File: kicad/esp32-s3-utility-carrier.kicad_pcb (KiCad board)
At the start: 2 copper layers, 90 x 65 mm, 27 parts, among them SW1 BTN1, SW2 BTN2, SW3 BTN3, U2 SN74AHCT125N

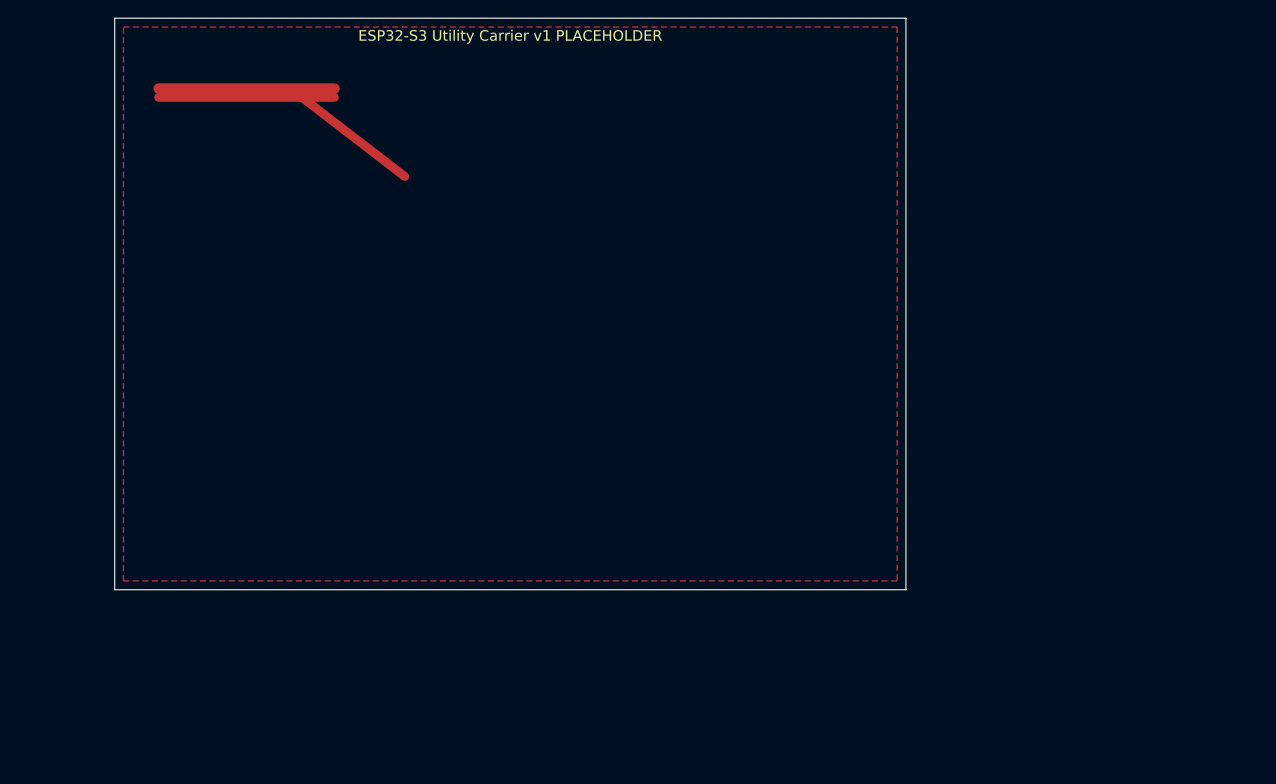
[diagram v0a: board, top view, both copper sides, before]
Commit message: feat(pcb): add optional W5500 ethernet header
v0.2 placeholder: J_W5500 (NOT POPULATED), 4 LED outputs via AHCT,
SPI on GPIO5/13/14/47/4/39 without pin conflicts; docs and generator updated.

Co-authored-by: Cursor <cursoragent@cursor.com>
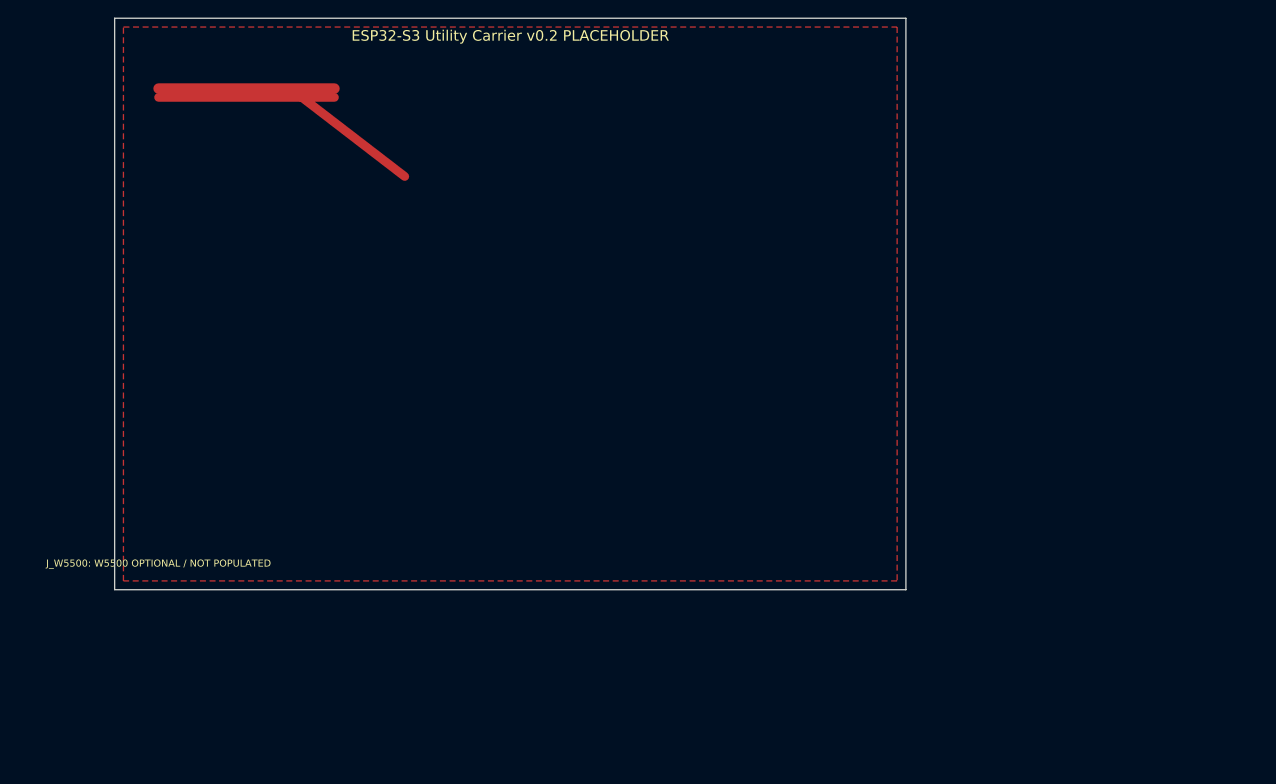
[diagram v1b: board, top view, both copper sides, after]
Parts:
- removed J_GPIO: GPIO, carrier:JST_XH_1x08_Placeholder
- added J_W5500: W5500_OPT_NP, carrier:JST_W5500_1x08_Placeholder, F.Cu at (5.00, 62.0)
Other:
- board text added: "ESP32-S3 Utility Carrier v0.2 PLACEHOLDER"
- board text added: "J_W5500: W5500 OPTIONAL / NOT POPULATED"
- board text removed: "ESP32-S3 Utility Carrier v1 PLACEHOLDER"
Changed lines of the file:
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@@
   (net 25 "ENC_DT")
   (net 26 "ENC_SW")
+  (net 27 "SPI_SCK")
+  (net 28 "SPI_MOSI")
+  (net 29 "SPI_MISO")
+  (net 30 "ETH_CS")
+  (net 31 "ETH_RST")
+  (net 32 "ETH_INT")
   (gr_rect (start 0 0) (end 90 65) (stroke (width 0.15) (type default)) (fill none) (layer "Edge.Cuts"))
   (gr_rect (start 28 8) (end 62 58) (stroke (width 0.2) (type default)) (fill none) (layer "Dwgs.User"))
@@
   (gr_text "ANTENNA KEEP-OUT" (at 45 64 0) (layer "Dwgs.User")
     (effects (font (size 0.9 0.9) (thickness 0.12))))
-  (gr_text "ESP32-S3 Utility Carrier v1 PLACEHOLDER" (at 45 2 0) (layer "F.SilkS")
+  (gr_text "ESP32-S3 Utility Carrier v0.2 PLACEHOLDER" (at 45 2 0) (layer "F.SilkS")
     (effects (font (size 1.2 1.2) (thickness 0.15))))
+  (gr_text "J_W5500: W5500 OPTIONAL / NOT POPULATED" (at 5 62 0) (layer "F.SilkS")
+    (effects (font (size 0.8 0.8) (thickness 0.1))))
   (footprint "carrier:JST_VH_1x02_Placeholder" (version 20240108) (generator "pcbnew")
     (layer "F.Cu") (at 5 8)
@@
     (attr through_hole)
   )
-  (footprint "carrier:JST_XH_1x08_Placeholder" (version 20240108) (generator "pcbnew")
-    (layer "F.Cu") (at 70 62)
-    (descr "") (tags "") (property "Reference" "J_GPIO")
-    (property "Value" "GPIO")
-    (property "Footprint" "carrier:JST_XH_1x08_Placeholder")
-    (attr through_hole)
-  )
+  (footprint "carrier:JST_W5500_1x08_Placeholder" (version 20240108) (generator "pcbnew")
+    (layer "F.Cu") (at 5 62)
+    (descr "") (tags "") (property "Reference" "J_W5500")
+    (property "Value" "W5500_OPT_NP")
+    (property "Footprint" "carrier:JST_W5500_1x08_Placeholder")
+    (attr through_hole)
+  )

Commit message: fix(pcb): clean up placeholder layout
Reorganize zones, keep connectors inside outline, add zone silk labels,
remove diagonal placeholder copper; layout verified in generator.

Co-authored-by: Cursor <cursoragent@cursor.com>
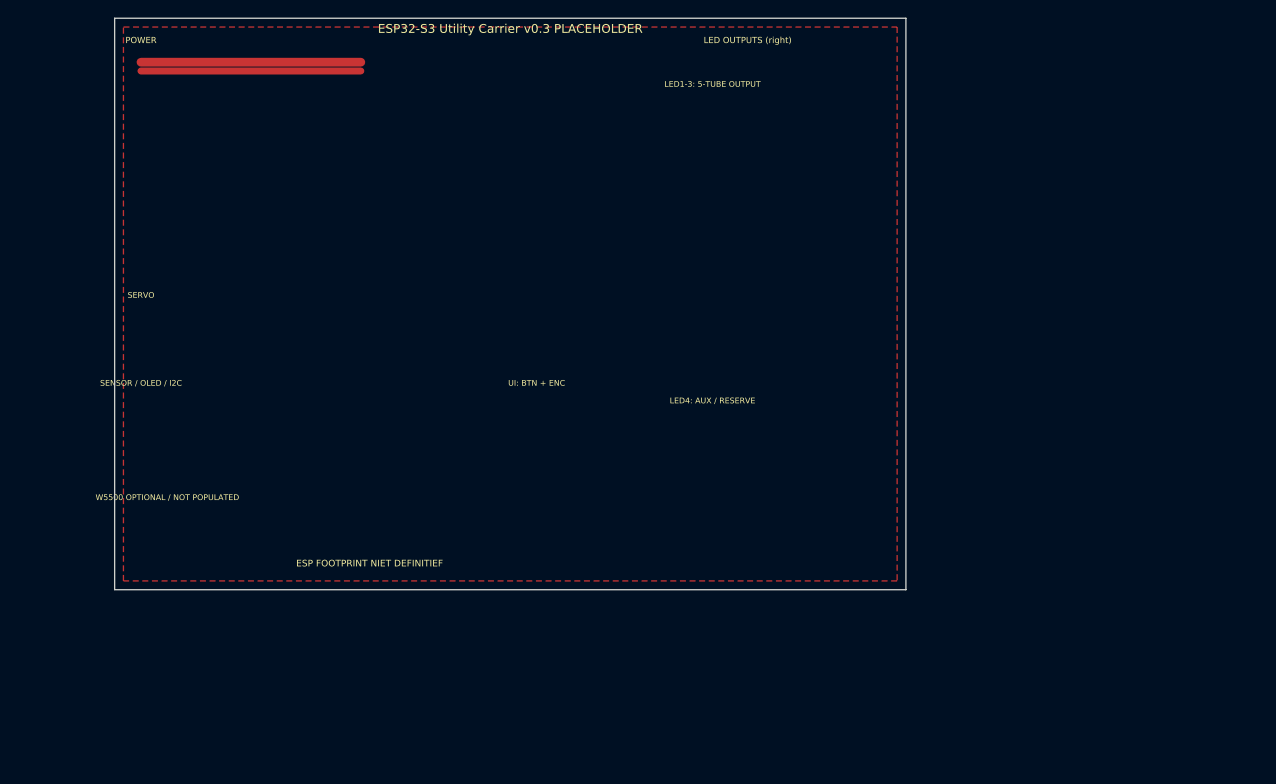
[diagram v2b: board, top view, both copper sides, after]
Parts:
- J_LED4: value LED4 -> LED4_AUX
- moved J_ENC 24.0 mm to (58.0, 56.0)
- moved SW1 22.2 mm to (48.0, 48.0)
- moved SW2 22.2 mm to (56.0, 48.0)
- moved SW3 22.2 mm to (64.0, 48.0)
- moved J_BTN 22.0 mm to (48.0, 56.0)
- moved J_SERVO2 21.4 mm to (11.0, 34.0)
- moved J_SERVO1 21.1 mm to (3.00, 34.0)
- moved J_LED4 19.7 mm to (78.0, 40.0)
- moved R_LED4 17.2 mm to (68.0, 40.0)
- moved J_LED3 16.4 mm to (78.0, 30.0)
- moved U2 16.1 mm to (54.0, 14.0)
- moved R_LED3 14.1 mm to (68.0, 30.0)
- moved J_OLED_EXT 13.9 mm to (12.0, 44.0)
- moved J_LED2 13.5 mm to (78.0, 20.0)
- moved J_I2C 12.4 mm to (21.0, 44.0)
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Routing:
- net 5V_LED: track 16.4 -> 0.00 mm
- net GND: track 20.0 -> 25.0 mm
- net 5V_MAIN: track 20.0 -> 25.0 mm
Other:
- board text added: "ESP FOOTPRINT NIET DEFINITIEF"
- board text added: "ESP32-S3 Utility Carrier v0.3 PLACEHOLDER"
- board text added: "LED OUTPUTS (right)"
- board text added: "LED1-3: 5-TUBE OUTPUT"
- board text added: "LED4: AUX / RESERVE"
- board text added: "POWER"
- board text added: "SENSOR / OLED / I2C"
- board text added: "SERVO"
- board text added: "UI: BTN + ENC"
- board text added: "USB KEEP-OUT"
- board text added: "W5500 OPTIONAL / NOT POPULATED"
- board text removed: "ESP32-S3 Utility Carrier v0.2 PLACEHOLDER"
- board text removed: "J_W5500: W5500 OPTIONAL / NOT POPULATED"
- board text removed: "USB KEEP-OUT (placeholder)"

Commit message: fix(pcb): improve placeholder layout
100x70 mm board with zoned placement, M3 mounts, readable silk,
no signal routing (airwires only), connectors inside margins.

Co-authored-by: Cursor <cursoragent@cursor.com>
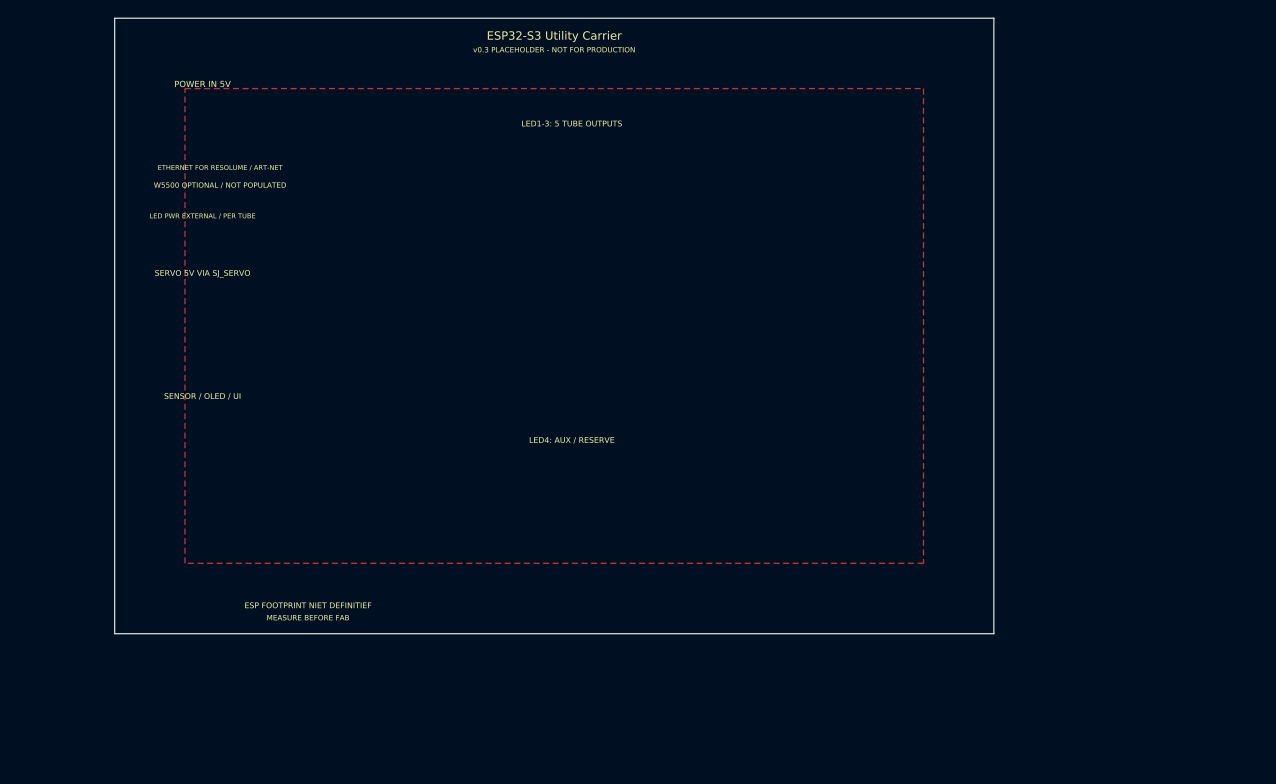
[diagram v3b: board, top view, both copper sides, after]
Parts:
- added H1: M3, carrier:M3_MountingHole, F.Cu at (9.00, 9.00)
- added H2: M3, carrier:M3_MountingHole, F.Cu at (91.0, 9.00)
- added H3: M3, carrier:M3_MountingHole, F.Cu at (9.00, 61.0)
- added H4: M3, carrier:M3_MountingHole, F.Cu at (91.0, 61.0)
- moved J_W5500 51.0 mm to (22.0, 8.00)
- moved SJ_SERVO 30.8 mm to (10.0, 34.0)
- moved C_SERVO 30.3 mm to (20.0, 34.0)
- moved J_LED4 14.4 mm to (86.0, 52.0)
- moved J_I2C 14.3 mm to (34.0, 50.0)
- moved J_LED3 12.8 mm to (86.0, 40.0)
- moved R_LED4 12.6 mm to (72.0, 52.0)
- moved C_MAIN 11.7 mm to (20.0, 10.0)
- moved F_OLED 11.7 mm to (22.0, 58.0)
- moved J_OLED_EXT 11.7 mm to (22.0, 50.0)
- moved J_LED2 11.3 mm to (86.0, 28.0)
- moved SW1 11.3 mm to (40.0, 56.0)
- moved R_LED3 10.8 mm to (72.0, 40.0)
- moved J_BTN 10.0 mm to (40.0, 62.0)
- moved J_LED1 10.0 mm to (86.0, 16.0)
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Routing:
- net GND: track 25.0 -> 0.00 mm
- net 5V_MAIN: track 25.0 -> 0.00 mm
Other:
- board size 90 x 65 mm -> 100 x 70 mm
- board text added: "ESP32-S3 Utility Carrier"
- board text added: "ETHERNET FOR RESOLUME / ART-NET"
- board text added: "LED PWR EXTERNAL / PER TUBE"
- board text added: "LED1-3: 5 TUBE OUTPUTS"
- board text added: "MEASURE BEFORE FAB"
- board text added: "POWER IN 5V"
- board text added: "SENSOR / OLED / UI"
- board text added: "SERVO 5V VIA SJ_SERVO"
- board text added: "v0.3 PLACEHOLDER - NOT FOR PRODUCTION"
- board text removed: "ESP32-S3 Utility Carrier v0.3 PLACEHOLDER"
- board text removed: "LED OUTPUTS (right)"
- board text removed: "LED1-3: 5-TUBE OUTPUT"
- board text removed: "POWER"
- board text removed: "SENSOR / OLED / I2C"
- board text removed: "SERVO"
- board text removed: "UI: BTN + ENC"

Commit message: fix(pcb): reset placeholder layout for readability
v0.4: 110x75 mm board, grouped placement, minimal keep-outs,
no copper pours or tracks, small zone silk labels only.

Co-authored-by: Cursor <cursoragent@cursor.com>
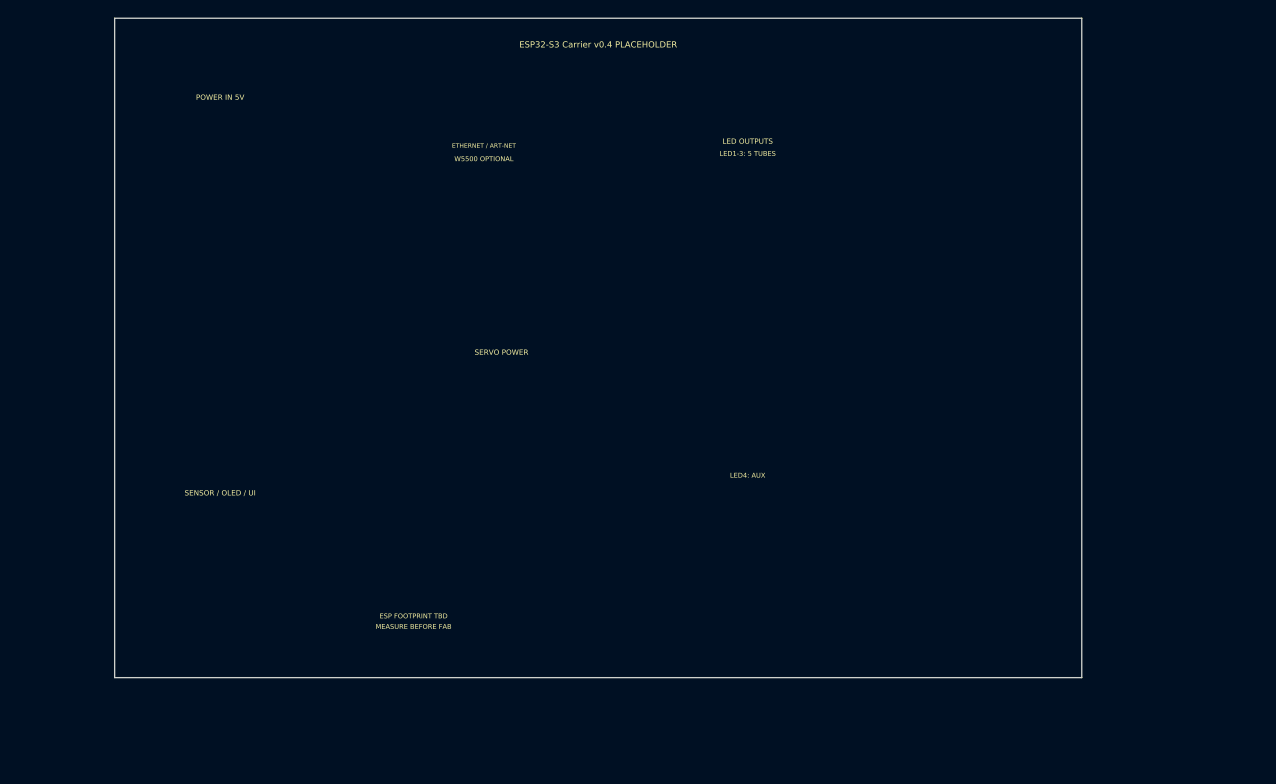
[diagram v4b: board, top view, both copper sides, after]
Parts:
- moved J_SERVO2 36.2 mm to (54.0, 42.0)
- moved J_SERVO1 34.2 mm to (44.0, 42.0)
- moved C_SERVO 34.0 mm to (54.0, 34.0)
- moved SJ_SERVO 34.0 mm to (44.0, 34.0)
- moved J_ENC 26.1 mm to (78.0, 60.0)
- moved J_W5500 20.1 mm to (42.0, 10.0)
- moved C_AHCT 14.6 mm to (80.0, 42.0)
- moved J_LED1 14.6 mm to (100.0, 20.0)
- moved J_LED2 14.6 mm to (100.0, 32.0)
- moved J_LED3 14.6 mm to (100.0, 44.0)
- moved J_LED4 14.6 mm to (100.0, 56.0)
- moved R_LED1 14.6 mm to (86.0, 20.0)
- moved R_LED2 14.6 mm to (86.0, 32.0)
- moved R_LED3 14.6 mm to (86.0, 44.0)
- moved R_LED4 14.6 mm to (86.0, 56.0)
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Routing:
- removed copper zone on F.Cu, net GND
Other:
- board size 100 x 70 mm -> 110 x 75 mm
- board text added: "ANT"
- board text added: "ESP FOOTPRINT TBD"
- board text added: "ESP32-S3 Carrier v0.4 PLACEHOLDER"
- board text added: "ETHERNET / ART-NET"
- board text added: "LED OUTPUTS"
- board text added: "LED1-3: 5 TUBES"
- board text added: "LED4: AUX"
- board text added: "SERVO POWER"
- board text added: "USB"
- board text added: "W5500 OPTIONAL"
- board text removed: "ANTENNA KEEP-OUT"
- board text removed: "ESP FOOTPRINT NIET DEFINITIEF"
- board text removed: "ESP32-S3 Utility Carrier"
- board text removed: "ETHERNET FOR RESOLUME / ART-NET"
- board text removed: "LED PWR EXTERNAL / PER TUBE"
- board text removed: "LED1-3: 5 TUBE OUTPUTS"
- board text removed: "LED4: AUX / RESERVE"
- board text removed: "SERVO 5V VIA SJ_SERVO"
- board text removed: "USB KEEP-OUT"
- board text removed: "W5500 OPTIONAL / NOT POPULATED"
- board text removed: "v0.3 PLACEHOLDER - NOT FOR PRODUCTION"

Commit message: feat(pcb): align layout to zone diagram
v0.5: 130x85 mm board, six dashed zone guides, component placement
per user diagram; airwires only, no copper pours.

Co-authored-by: Cursor <cursoragent@cursor.com>
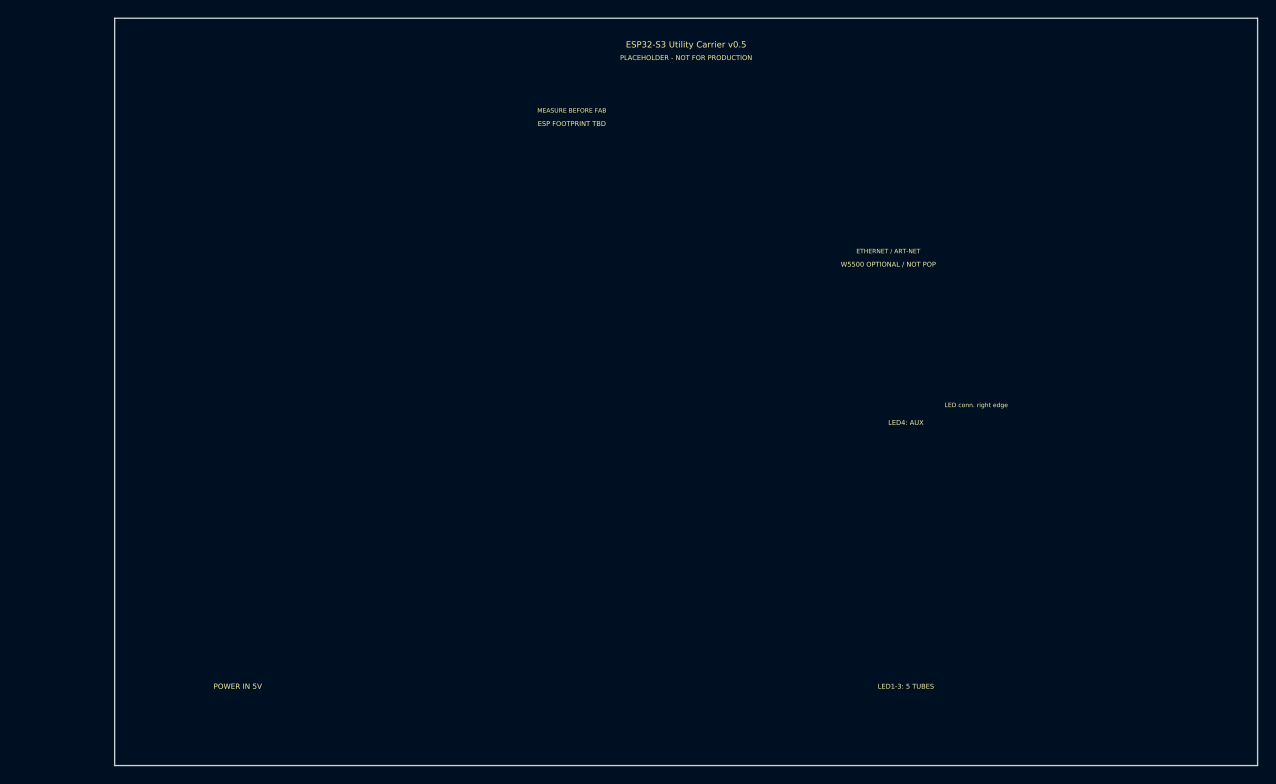
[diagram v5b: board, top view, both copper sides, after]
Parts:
- moved C_MAIN 60.1 mm to (26.0, 72.0)
- moved J_MAIN 60.0 mm to (14.0, 72.0)
- moved J_LED1 55.7 mm to (120.0, 72.0)
- moved R_LED1 55.7 mm to (106.0, 72.0)
- moved J_ENC 53.7 mm to (40.0, 22.0)
- moved SW1 51.0 mm to (14.0, 24.0)
- moved SW2 51.0 mm to (24.0, 24.0)
- moved SW3 51.0 mm to (34.0, 24.0)
- moved J_W5500 46.0 mm to (88.0, 12.0)
- moved J_I2C 44.0 mm to (38.0, 14.0)
- moved J_LD2450 44.0 mm to (14.0, 14.0)
- moved J_OLED_EXT 44.0 mm to (26.0, 14.0)
- moved J_BTN 38.8 mm to (14.0, 30.0)
- moved J_LED2 37.7 mm to (120.0, 64.0)
- moved R_LED2 37.7 mm to (106.0, 64.0)
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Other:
- board size 110 x 75 mm -> 130 x 85 mm
- board text added: "1 POWER"
- board text added: "2 ESP32-S3 DEVKIT"
- board text added: "3 LED OUTPUTS"
- board text added: "4 SENSOR / OLED / UI"
- board text added: "5 SERVO POWER"
- board text added: "6 W5500 / ETHERNET"
- board text added: "ANT keep-out"
- board text added: "ESP32-S3 Utility Carrier v0.5"
- board text added: "LED conn. right edge"
- board text added: "PLACEHOLDER - NOT FOR PRODUCTION"
- board text added: "USB edge"
- board text added: "W5500 OPTIONAL / NOT POP"
- board text removed: "ANT"
- board text removed: "ESP32-S3 Carrier v0.4 PLACEHOLDER"
- board text removed: "LED OUTPUTS"
- board text removed: "SENSOR / OLED / UI"
- board text removed: "SERVO POWER"
- board text removed: "USB"
- board text removed: "W5500 OPTIONAL"
